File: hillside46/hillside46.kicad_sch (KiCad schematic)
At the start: 93 parts, among them J1 I2C, J2 TRRS, J3 Bat_Pos, J4 Bat_Neg, J5 XF2M-1215-1A, K1 SW_Key, K10 SW_Key, K11 SW_Key, K12 SW_Key, K13 SW_Key, K14 SW_Key, K15 SW_Key, K16 SW_Key, K17 SW_Key, K18 SW_Key, K19 SW_Rotary, K2 SW_Key, K20 SW_Rotary, K21 SW_Key, K22 SW_Key, K23 SW_Key, K3 SW_Key, K4 SW_Key, K5 SW_Key, K6 SW_Key, K7 SW_Key, K8 SW_Key, K9 SW_Key, SW1 SKQGAFE010, SW2 SW_Power, U1 NiceNano2_r, U2 SRV05-4

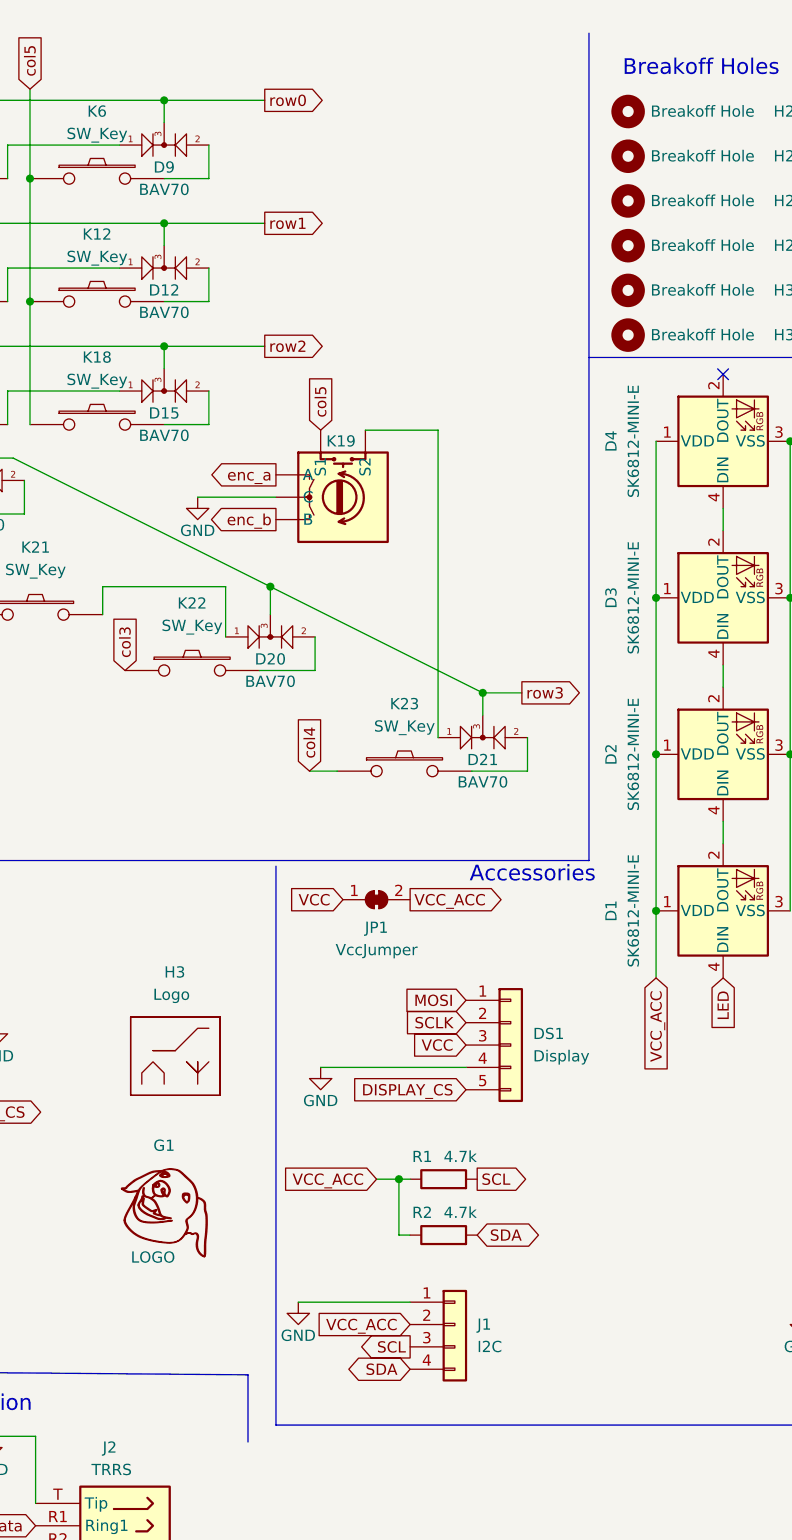
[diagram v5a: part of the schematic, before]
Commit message: Flipping nice nano vias for bottom mount, removed I2C headers, moved edge cut closer to the nice nano edge
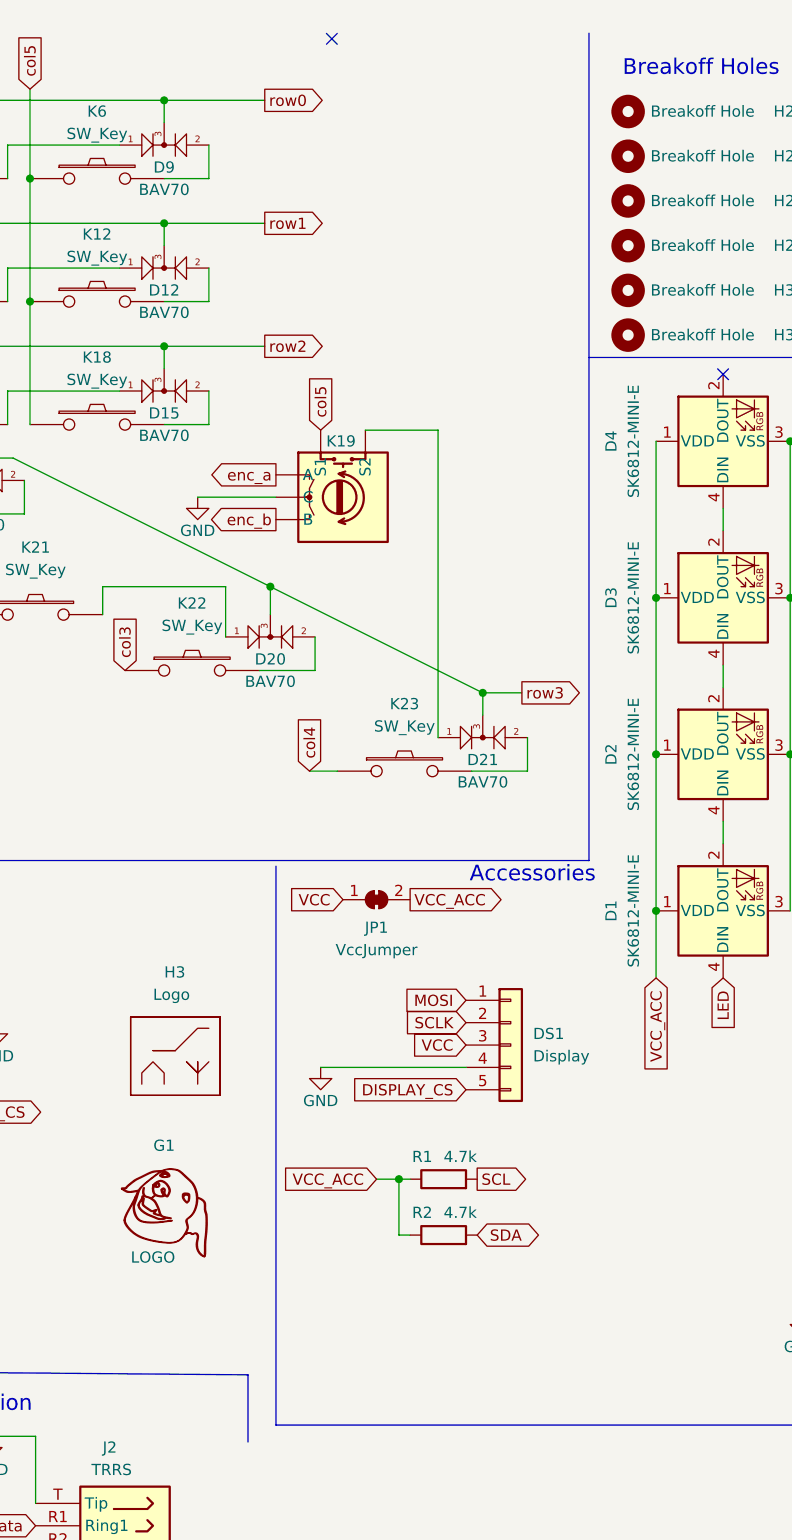
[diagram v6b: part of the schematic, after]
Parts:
- removed J1: I2C, Connector_PinHeader_2.54mm:PinHeader_1x04_P2.54mm_Vertical, symbol Connector_Generic:Conn_01x04
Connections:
- no-connect marks 13 -> 14
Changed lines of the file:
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@@
     (title "Hillside View 46 Keyboard")
     (date "2022-10-13")
-    (rev "0.2.0")
+    (rev "0.3.0")
     (company "ExAF")
     (comment 1 "SPI headers for the nice!view display and 12 pin connector for an I2C cirque trackpad")
@@
   (no_connect (at 213.36 50.8))
   (no_connect (at 99.06 154.94))
+  (no_connect (at 168.91 12.7))
   (no_connect (at 60.96 182.88))
   (no_connect (at 135.255 184.15))
@@
     (stroke (width 0) (type default) (color 0 0 0 0))
   )
-  (wire (pts (xy 165.1 156.21) (xy 177.8 156.21))
-    (stroke (width 0) (type default) (color 0 0 0 0))
-  )
   (wire (pts (xy 47.625 55.245) (xy 56.515 47.625))
     (stroke (width 0) (type default) (color 0 0 0 0))
@@
     )
   )
-  (global_label "VCC_ACC" (shape input) (at 177.8 158.75 180) (fields_autoplaced)
-    (effects (font (size 1.27 1.27)) (justify right))
-    (property "Intersheet References" "${INTERSHEET_REFS}" (id 0) (at 2.54 27.94 0)
-      (effects (font (size 1.27 1.27)) hide)
-    )
-  )
   (global_label "DISPLAY_CS" (shape input) (at 184.15 132.08 180) (fields_autoplaced)
     (effects (font (size 1.27 1.27)) (justify right))
@@
     )
   )
-  (global_label "SDA" (shape bidirectional) (at 177.8 163.83 180) (fields_autoplaced)
-    (effects (font (size 1.27 1.27)) (justify right))
-    (property "Intersheet References" "${INTERSHEET_REFS}" (id 0) (at 364.49 300.99 0)
-      (effects (font (size 1.27 1.27)) hide)
-    )
-  )
   (global_label "row3" (shape output) (at 190.5 86.995 0) (fields_autoplaced)
     (effects (font (size 1.27 1.27)) (justify left))
@@
     )
   )
-  (global_label "SCL" (shape output) (at 177.8 161.29 180) (fields_autoplaced)
-    (effects (font (size 1.27 1.27)) (justify right))
-    (property "Intersheet References" "${INTERSHEET_REFS}" (id 0) (at 364.49 292.1 0)
-      (effects (font (size 1.27 1.27)) hide)
-    )
-  )
   (global_label "enc_b" (shape output) (at 162.56 67.31 180) (fields_autoplaced)
     (effects (font (size 1.27 1.27)) (justify right))
@@
     (pin "1")
   )
-  (symbol (lib_id "Connector_Generic:Conn_01x04") (at 182.88 158.75 0) (unit 1)
-    (in_bom yes) (on_board yes) (fields_autoplaced)
-    (property "Reference" "J1" (id 0) (at 185.42 158.7499 0)
-      (effects (font (size 1.27 1.27)) (justify left))
-    )
-    (property "Value" "I2C" (id 1) (at 185.42 161.2899 0)
-      (effects (font (size 1.27 1.27)) (justify left))
-    )
-    (property "Footprint" "Connector_PinHeader_2.54mm:PinHeader_1x04_P2.54mm_Vertical" (id 2) (at 182.88 158.75 0)
-      (effects (font (size 1.27 1.27)) hide)
-    )
-    (property "Datasheet" "~" (id 3) (at 182.88 158.75 0)
-      (effects (font (size 1.27 1.27)) hide)
-    )
-    (pin "1")
-    (pin "2")
-    (pin "3")
-    (pin "4")
-  )
   (symbol (lib_id "hillside:TRRS") (at 137.795 181.61 0) (unit 1)
     (in_bom yes) (on_board yes)
@@
     (pin "2")
   )
-  (symbol (lib_id "power:GND") (at 165.1 156.21 0) (unit 1)
-    (in_bom yes) (on_board yes)
-    (property "Reference" "#PWR012" (id 0) (at 165.1 162.56 0)
-      (effects (font (size 1.27 1.27)) hide)
-    )
-    (property "Value" "GND" (id 1) (at 165.1 160.02 0))
-    (property "Footprint" "" (id 2) (at 165.1 156.21 0)
-      (effects (font (size 1.27 1.27)) hide)
-    )
-    (property "Datasheet" "" (id 3) (at 165.1 156.21 0)
-      (effects (font (size 1.27 1.27)) hide)
-    )
-    (pin "1")
-  )
   (symbol (lib_id "power:GND") (at 130.175 171.45 0) (unit 1)
     (in_bom yes) (on_board yes)
@@
       (reference "#PWR011") (unit 1) (value "GND") (footprint "")
     )
-    (path "/67e88f8a-c114-48e4-9cf9-2e6abca58c7b"
-      (reference "#PWR012") (unit 1) (value "GND") (footprint "")
-    )
     (path "/7b23d84d-de1b-4b47-89b8-d59d8feef4f5"
       (reference "#PWR0101") (unit 1) (value "GND") (footprint "")
@@
       (reference "H31") (unit 1) (value "Breakoff Hole") (footprint "hillside_basic:HoleBreakoff_1mm")
     )
-    (path "/11ad1f74-709a-4d73-82dc-88c76de65682"
-      (reference "J1") (unit 1) (value "I2C") (footprint "Connector_PinHeader_2.54mm:PinHeader_1x04_P2.54mm_Vertical")
-    )
     (path "/1877e8f2-b5eb-4e12-bda7-600741d0d39f"

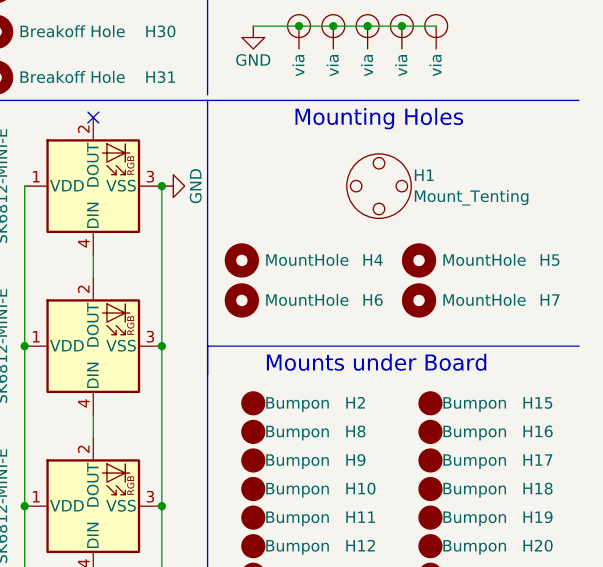
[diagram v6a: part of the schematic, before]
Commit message: Adding mounting holes for the display cover
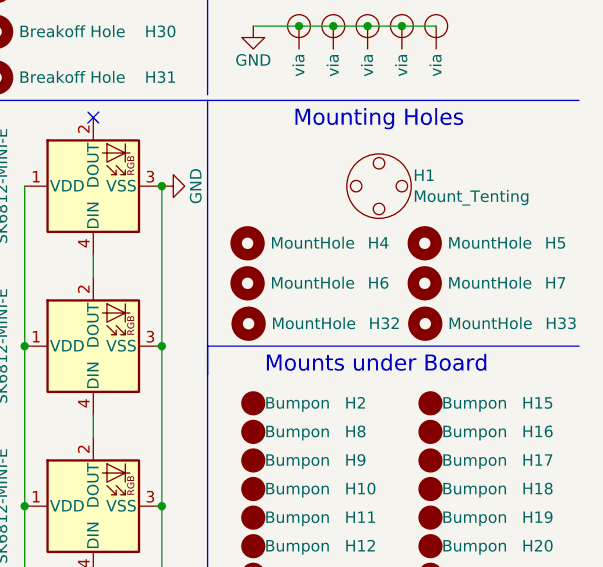
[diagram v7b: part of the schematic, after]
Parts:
- added H32, H33: MountHole, hillside:MountingHole_2.2mm_with_PCB_insert_rings, symbol Mechanical:MountingHole
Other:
- moved on the sheet: H4, H5, H6, H7
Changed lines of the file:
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@@
     )
   )
-  (symbol (lib_id "Mechanical:MountingHole") (at 249.555 66.675 0) (unit 1)
-    (in_bom yes) (on_board yes)
-    (property "Reference" "H5" (id 0) (at 262.89 66.675 0)
-      (effects (font (size 1.27 1.27)) (justify left))
-    )
-    (property "Value" "MountHole" (id 1) (at 252.095 66.675 0)
-      (effects (font (size 1.27 1.27)) (justify left))
-    )
-    (property "Footprint" "hillside:MountingHole_2.2mm_with_PCB_insert_rings" (id 2) (at 249.555 66.675 0)
-      (effects (font (size 1.27 1.27)) hide)
-    )
-    (property "Datasheet" "~" (id 3) (at 249.555 66.675 0)
-      (effects (font (size 1.27 1.27)) hide)
-    )
-    (property "Config" "do not fit" (id 4) (at 249.555 66.675 0)
-      (effects (font (size 1.27 1.27)) hide)
-    )
-  )
-  (symbol (lib_id "Mechanical:MountingHole") (at 229.87 66.675 0) (unit 1)
-    (in_bom yes) (on_board yes)
-    (property "Reference" "H4" (id 0) (at 243.205 66.675 0)
-      (effects (font (size 1.27 1.27)) (justify left))
-    )
-    (property "Value" "MountHole" (id 1) (at 232.41 66.675 0)
-      (effects (font (size 1.27 1.27)) (justify left))
-    )
-    (property "Footprint" "hillside:MountingHole_2.2mm_with_PCB_insert_rings" (id 2) (at 229.87 66.675 0)
-      (effects (font (size 1.27 1.27)) hide)
-    )
-    (property "Datasheet" "~" (id 3) (at 229.87 66.675 0)
-      (effects (font (size 1.27 1.27)) hide)
-    )
-    (property "Config" "do not fit" (id 4) (at 229.87 66.675 0)
-      (effects (font (size 1.27 1.27)) hide)
-    )
-  )
-  (symbol (lib_id "Mechanical:MountingHole") (at 229.87 71.12 0) (unit 1)
-    (in_bom yes) (on_board yes)
-    (property "Reference" "H6" (id 0) (at 243.205 71.12 0)
-      (effects (font (size 1.27 1.27)) (justify left))
-    )
-    (property "Value" "MountHole" (id 1) (at 232.41 71.12 0)
-      (effects (font (size 1.27 1.27)) (justify left))
-    )
-    (property "Footprint" "hillside:MountingHole_2.2mm_with_PCB_insert_rings" (id 2) (at 229.87 71.12 0)
-      (effects (font (size 1.27 1.27)) hide)
-    )
-    (property "Datasheet" "~" (id 3) (at 229.87 71.12 0)
-      (effects (font (size 1.27 1.27)) hide)
-    )
-    (property "Config" "do not fit" (id 4) (at 229.87 71.12 0)
-      (effects (font (size 1.27 1.27)) hide)
-    )
-  )
-  (symbol (lib_id "Mechanical:MountingHole") (at 249.555 71.12 0) (unit 1)
-    (in_bom yes) (on_board yes)
-    (property "Reference" "H7" (id 0) (at 262.89 71.12 0)
-      (effects (font (size 1.27 1.27)) (justify left))
-    )
-    (property "Value" "MountHole" (id 1) (at 252.095 71.12 0)
-      (effects (font (size 1.27 1.27)) (justify left))
-    )
-    (property "Footprint" "hillside:MountingHole_2.2mm_with_PCB_insert_rings" (id 2) (at 249.555 71.12 0)
-      (effects (font (size 1.27 1.27)) hide)
-    )
-    (property "Datasheet" "~" (id 3) (at 249.555 71.12 0)
-      (effects (font (size 1.27 1.27)) hide)
-    )
-    (property "Config" "do not fit" (id 4) (at 249.555 71.12 0)
+  (symbol (lib_id "Mechanical:MountingHole") (at 250.19 64.77 0) (unit 1)
+    (in_bom yes) (on_board yes)
+    (property "Reference" "H5" (id 0) (at 263.525 64.77 0)
+      (effects (font (size 1.27 1.27)) (justify left))
+    )
+    (property "Value" "MountHole" (id 1) (at 252.73 64.77 0)
+      (effects (font (size 1.27 1.27)) (justify left))
+    )
+    (property "Footprint" "hillside:MountingHole_2.2mm_with_PCB_insert_rings" (id 2) (at 250.19 64.77 0)
+      (effects (font (size 1.27 1.27)) hide)
+    )
+    (property "Datasheet" "~" (id 3) (at 250.19 64.77 0)
+      (effects (font (size 1.27 1.27)) hide)
+    )
+    (property "Config" "do not fit" (id 4) (at 250.19 64.77 0)
+      (effects (font (size 1.27 1.27)) hide)
+    )
+  )
+  (symbol (lib_id "Mechanical:MountingHole") (at 230.505 64.77 0) (unit 1)
+    (in_bom yes) (on_board yes)
+    (property "Reference" "H4" (id 0) (at 243.84 64.77 0)
+      (effects (font (size 1.27 1.27)) (justify left))
+    )
+    (property "Value" "MountHole" (id 1) (at 233.045 64.77 0)
+      (effects (font (size 1.27 1.27)) (justify left))
+    )
+    (property "Footprint" "hillside:MountingHole_2.2mm_with_PCB_insert_rings" (id 2) (at 230.505 64.77 0)
+      (effects (font (size 1.27 1.27)) hide)
+    )
+    (property "Datasheet" "~" (id 3) (at 230.505 64.77 0)
+      (effects (font (size 1.27 1.27)) hide)
+    )
+    (property "Config" "do not fit" (id 4) (at 230.505 64.77 0)
+      (effects (font (size 1.27 1.27)) hide)
+    )
+  )
+  (symbol (lib_id "Mechanical:MountingHole") (at 230.505 69.215 0) (unit 1)
+    (in_bom yes) (on_board yes)
+    (property "Reference" "H6" (id 0) (at 243.84 69.215 0)
+      (effects (font (size 1.27 1.27)) (justify left))
+    )
+    (property "Value" "MountHole" (id 1) (at 233.045 69.215 0)
+      (effects (font (size 1.27 1.27)) (justify left))
+    )
+    (property "Footprint" "hillside:MountingHole_2.2mm_with_PCB_insert_rings" (id 2) (at 230.505 69.215 0)
+      (effects (font (size 1.27 1.27)) hide)
+    )
+    (property "Datasheet" "~" (id 3) (at 230.505 69.215 0)
+      (effects (font (size 1.27 1.27)) hide)
+    )
+    (property "Config" "do not fit" (id 4) (at 230.505 69.215 0)
+      (effects (font (size 1.27 1.27)) hide)
+    )
+  )
+  (symbol (lib_id "Mechanical:MountingHole") (at 250.19 69.215 0) (unit 1)
+    (in_bom yes) (on_board yes)
+    (property "Reference" "H7" (id 0) (at 263.525 69.215 0)
+      (effects (font (size 1.27 1.27)) (justify left))
+    )
+    (property "Value" "MountHole" (id 1) (at 252.73 69.215 0)
+      (effects (font (size 1.27 1.27)) (justify left))
+    )
+    (property "Footprint" "hillside:MountingHole_2.2mm_with_PCB_insert_rings" (id 2) (at 250.19 69.215 0)
+      (effects (font (size 1.27 1.27)) hide)
+    )
+    (property "Datasheet" "~" (id 3) (at 250.19 69.215 0)
+      (effects (font (size 1.27 1.27)) hide)
+    )
+    (property "Config" "do not fit" (id 4) (at 250.19 69.215 0)
       (effects (font (size 1.27 1.27)) hide)
     )
@@
     (pin "2")
   )
+  (symbol (lib_id "Mechanical:MountingHole") (at 250.2463 73.7063 0) (unit 1)
+    (in_bom yes) (on_board yes)
+    (property "Reference" "H33" (id 0) (at 263.5813 73.7063 0)
+      (effects (font (size 1.27 1.27)) (justify left))
+    )
+    (property "Value" "MountHole" (id 1) (at 252.7863 73.7063 0)
+      (effects (font (size 1.27 1.27)) (justify left))
+    )
+    (property "Footprint" "hillside:MountingHole_2.2mm_with_PCB_insert_rings" (id 2) (at 250.2463 73.7063 0)
+      (effects (font (size 1.27 1.27)) hide)
+    )
+    (property "Datasheet" "~" (id 3) (at 250.2463 73.7063 0)
+      (effects (font (size 1.27 1.27)) hide)
+    )
+    (property "Config" "do not fit" (id 4) (at 250.2463 73.7063 0)
+      (effects (font (size 1.27 1.27)) hide)
+    )
+  )
   (symbol (lib_id "power:GND") (at 130.175 171.45 0) (unit 1)
     (in_bom yes) (on_board yes)
@@
     )
   )
+  (symbol (lib_id "Mechanical:MountingHole") (at 230.6181 73.7063 0) (unit 1)
+    (in_bom yes) (on_board yes)
+    (property "Reference" "H32" (id 0) (at 243.9531 73.7063 0)
+      (effects (font (size 1.27 1.27)) (justify left))
+    )
+    (property "Value" "MountHole" (id 1) (at 233.1581 73.7063 0)
+      (effects (font (size 1.27 1.27)) (justify left))
+    )
+    (property "Footprint" "hillside:MountingHole_2.2mm_with_PCB_insert_rings" (id 2) (at 230.6181 73.7063 0)
+      (effects (font (size 1.27 1.27)) hide)
+    )
+    (property "Datasheet" "~" (id 3) (at 230.6181 73.7063 0)
+      (effects (font (size 1.27 1.27)) hide)
+    )
+    (property "Config" "do not fit" (id 4) (at 230.6181 73.7063 0)
+      (effects (font (size 1.27 1.27)) hide)
+    )
+  )
   (symbol (lib_id "hillside_basic:Bumpon") (at 250.825 92.075 0) (unit 1)
     (in_bom no) (on_board yes) (fields_autoplaced)
@@
       (reference "H31") (unit 1) (value "Breakoff Hole") (footprint "hillside_basic:HoleBreakoff_1mm")
     )
+    (path "/e4b9a278-9c87-4f9d-838f-de3da4494b53"
+      (reference "H32") (unit 1) (value "MountHole") (footprint "hillside:MountingHole_2.2mm_with_PCB_insert_rings")
+    )
+    (path "/6e14de43-bb53-4684-ae1c-6f0c8e646b91"
+      (reference "H33") (unit 1) (value "MountHole") (footprint "hillside:MountingHole_2.2mm_with_PCB_insert_rings")
+    )
     (path "/1877e8f2-b5eb-4e12-bda7-600741d0d39f"
